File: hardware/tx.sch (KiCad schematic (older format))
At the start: 68 parts, among them J3 SMA, Q2 RE1C002UN, U12 ADF4158, U13 TLV172DCK, U14 PAT1220-3dB, U15 HMC431LP4, U16 PD4859J5050S2HF, U17 PAT1220-5dB, U18 SE5004L, U19 DC4759J5020AHF, U20 PAT1220-6dB

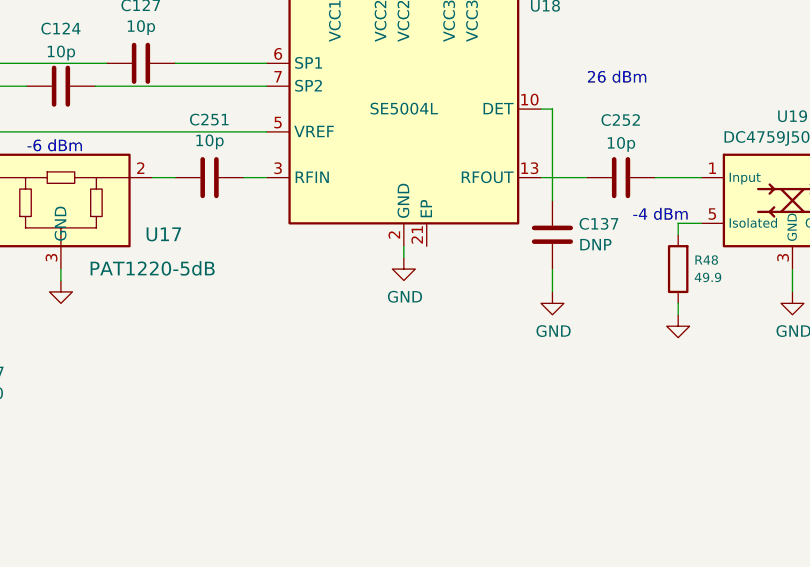
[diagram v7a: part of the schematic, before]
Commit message: Passes DRC.
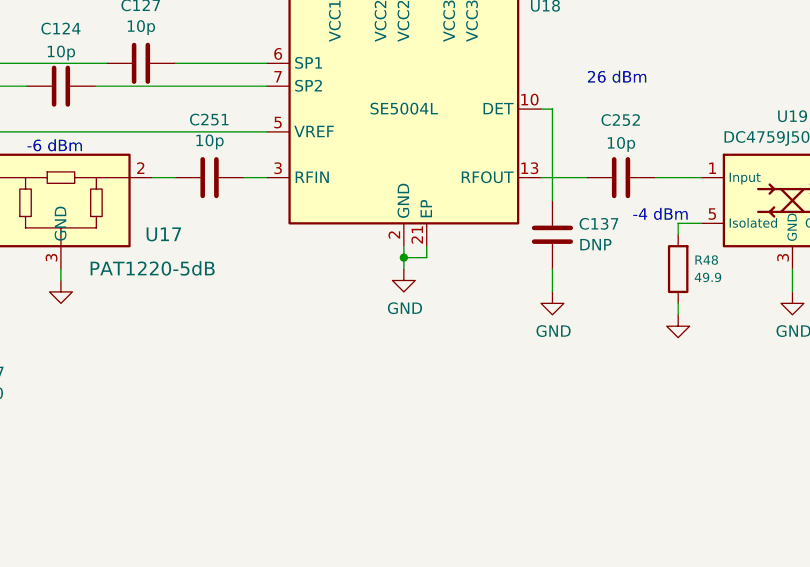
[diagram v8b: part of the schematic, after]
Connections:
- net GND: now also U18.21 (EP)
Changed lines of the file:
@@
 L power:GND #PWR0131
 U 1 1 5B5563FC
-P 12850 5350
-F 0 "#PWR0131" H 12850 5100 50  0001 C CNN
-F 1 "GND" H 12855 5177 50  0000 C CNN
-F 2 "" H 12850 5350 50  0001 C CNN
-F 3 "" H 12850 5350 50  0001 C CNN
-	1    12850 5350
+P 12850 5400
+F 0 "#PWR0131" H 12850 5150 50  0001 C CNN
+F 1 "GND" H 12855 5227 50  0000 C CNN
+F 2 "" H 12850 5400 50  0001 C CNN
+F 3 "" H 12850 5400 50  0001 C CNN
+	1    12850 5400
 	1    0    0    -1
 $EndComp
@@
 Wire Wire Line
 	4350 6850 4350 6900
-$Comp
-L RF:SE5004L U18
-U 1 1 5C136930
-P 12850 4700
-F 0 "U18" H 13400 5150 50  0000 L CNN
-F 1 "SE5004L" H 12700 4700 50  0000 L CNN
-F 2 "Package_DFN_QFN:QFN-20-1EP_4x4mm_P0.5mm_EP2.5x2.5mm" H 12750 4600 50  0001 C CNN
-F 3 "http://www.skyworksinc.com/uploads/documents/SE5004L_202393B.pdf" H 12850 4700 50  0001 C CNN
-F 4 "SE5004L-R" H 250 0   50  0001 C CNN "MFN"
-	1    12850 4700
-	1    0    0    -1
-$EndComp
 $Comp
 L Device:C C124
@@
 Wire Wire Line
 	11550 2700 11950 2700
+$Comp
+L RF:SE5004L U18
+U 1 1 5C136930
+P 12850 4700
+F 0 "U18" H 13400 5150 50  0000 L CNN
+F 1 "SE5004L" H 12700 4700 50  0000 L CNN
+F 2 "Package_DFN_QFN:QFN-20-1EP_4x4mm_P0.5mm_EP2.5x2.5mm" H 12750 4600 50  0001 C CNN
+F 3 "http://www.skyworksinc.com/uploads/documents/SE5004L_202393B.pdf" H 12850 4700 50  0001 C CNN
+F 4 "SE5004L-R" H 250 0   50  0001 C CNN "MFN"
+	1    12850 4700
+	1    0    0    -1
+$EndComp
+Wire Wire Line
+	12950 5300 12950 5350
+Wire Wire Line
+	12950 5350 12850 5350
+Connection ~ 12850 5350
+Wire Wire Line
+	12850 5400 12850 5350
 $EndSCHEMATC
